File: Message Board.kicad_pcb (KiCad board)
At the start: 2 copper layers, 182.9 x 99.1 mm, 45 parts, among them J1 Conn_01x02, Q1 LGE2300, Q2 LGE2300, SW1 SW_SPST, U1 esp32-c3, U2 LM1117-5.0, U3 LM1117-3.3, U4 epaper75

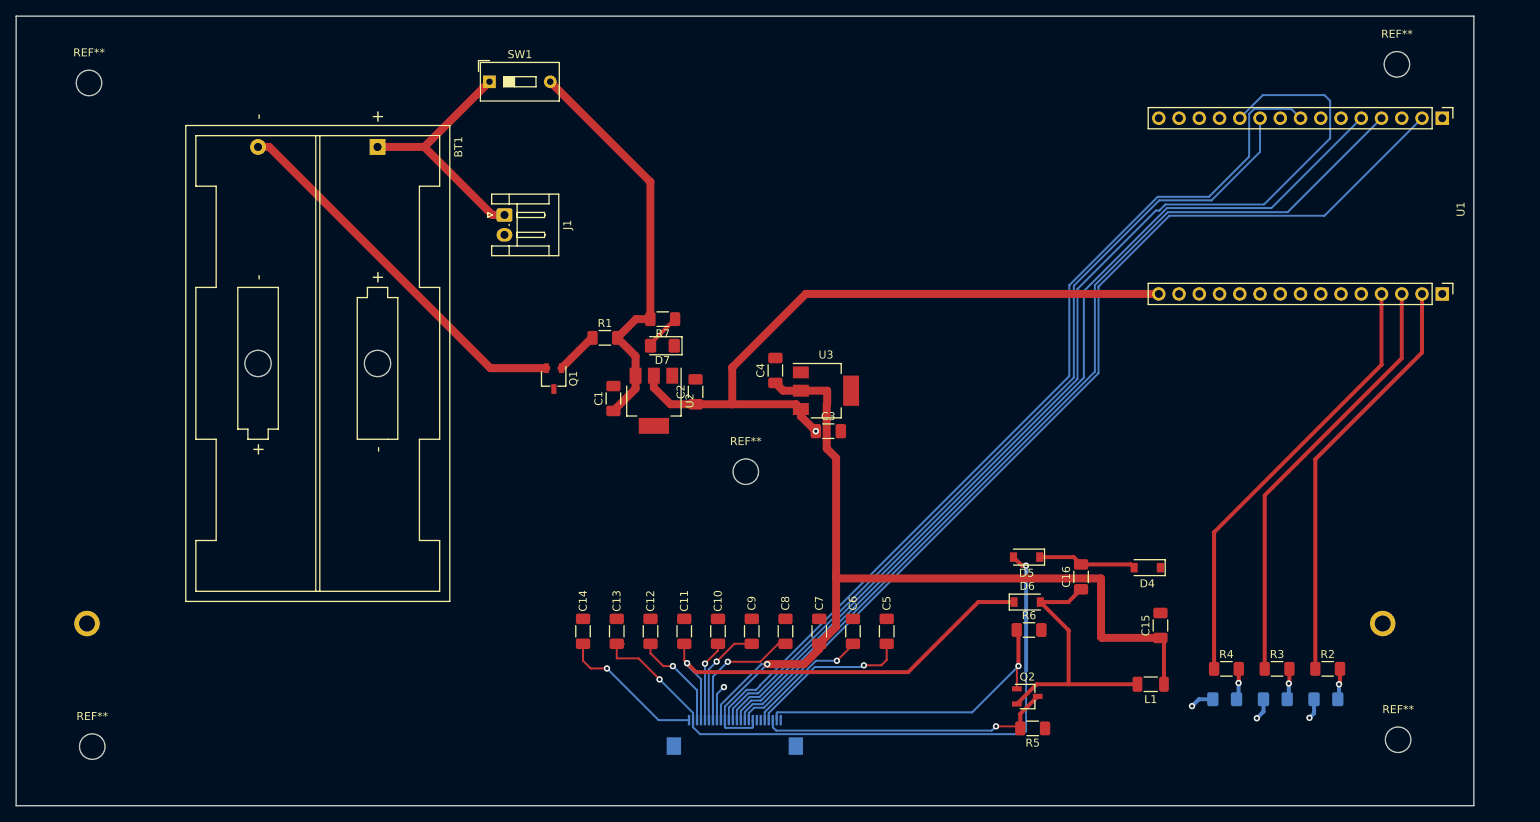
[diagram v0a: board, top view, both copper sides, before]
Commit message: Changed orientation of the FFC connector, battery from 2x18650 to 1x18650, devboard to ESP32-C3-DEVKITM-1 and updated the epaper footprint. Deleted second linear regualtor
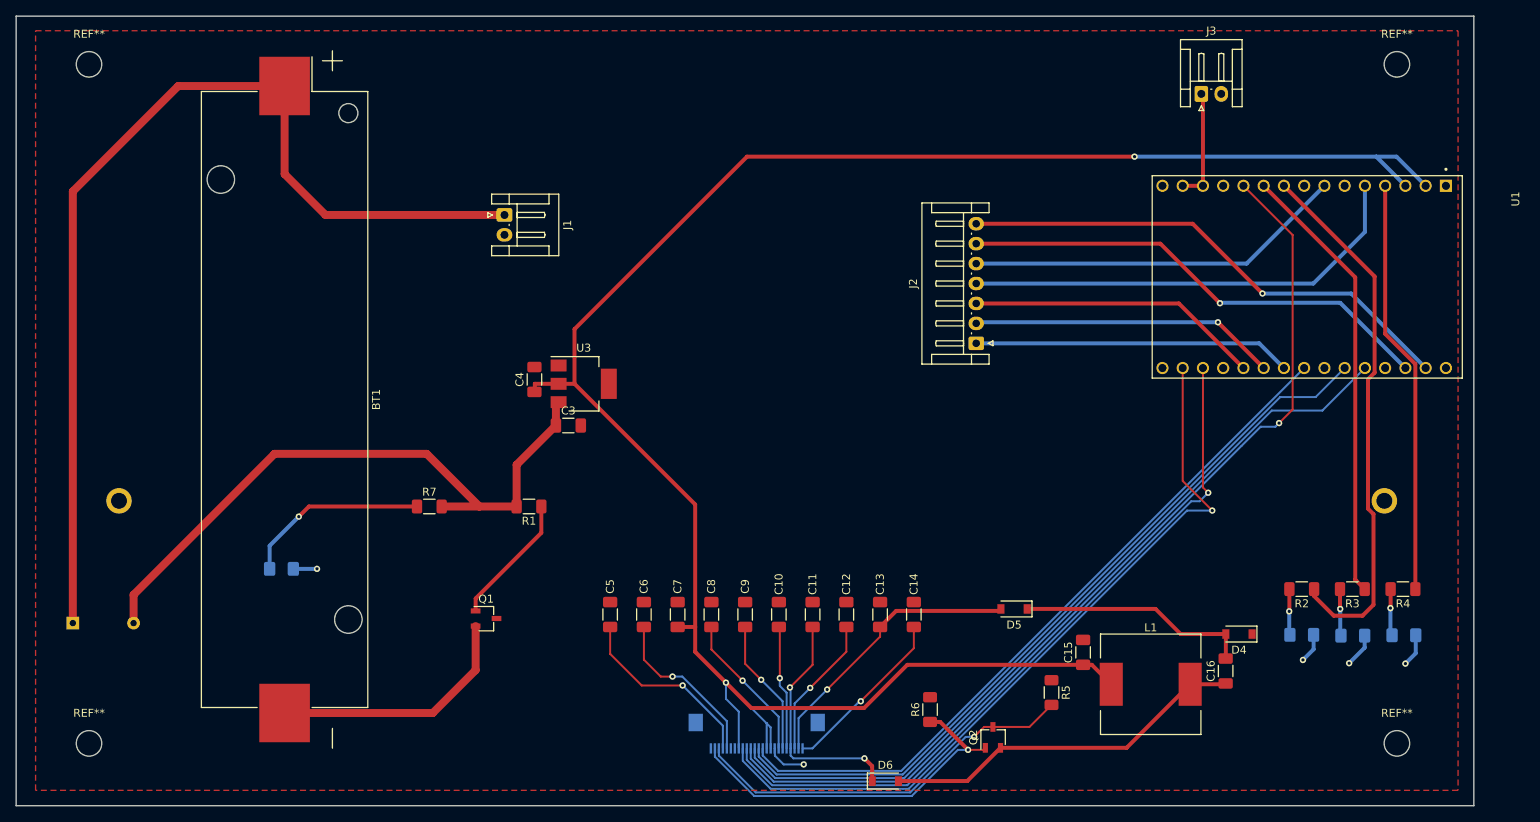
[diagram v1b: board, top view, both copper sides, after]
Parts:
- removed C1: 100nF, Capacitor_SMD:C_1206_3216Metric_Pad1.33x1.80mm_HandSolder
- removed C2: 10uF, Capacitor_SMD:C_1206_3216Metric_Pad1.33x1.80mm_HandSolder
- removed D3: LED, LED_SMD:LED_1206_3216Metric_Pad1.42x1.75mm_HandSolder
- removed the REF** at (162.7, 115.6)
- removed the REF** at (244.5, 149.2)
- removed the REF** at (80.7, 150.1)
- removed the REF** at (80.3, 66.8)
- removed U2: LM1117-5.0, Package_TO_SOT_SMD:SOT-223
- added D0: LED, LED_SMD:LED_1206_3216Metric_Pad1.42x1.75mm_HandSolder, B.Cu at (232.4, 136.0)
- added J2: Conn_01x07, Connector_JST:JST_EH_S7B-EH_1x07_P2.50mm_Horizontal, F.Cu at (191.6, 99.5)
- added J3: Conn_01x02, Connector_JST:JST_EH_S2B-EH_1x02_P2.50mm_Horizontal, F.Cu at (219.8, 68.2)
- added REF**: MountingHole_3.2mm_M3_DIN965, MountingHole:MountingHole_3.2mm_M3_DIN965, F.Cu at (244.3, 149.7)
- added REF**: MountingHole_3.2mm_M3_DIN965, MountingHole:MountingHole_3.2mm_M3_DIN965, F.Cu at (80.3, 149.7)
- added REF**: MountingHole_3.2mm_M3_DIN965, MountingHole:MountingHole_3.2mm_M3_DIN965, F.Cu at (80.3, 64.5)
- BT1: value 7.2 -> 3.6V; footprint Battery:BatteryHolder_Keystone_2462_2xAA -> Battery:BatteryHolder_Keystone_1042_1x18650
- D7, SW1: moved to B.Cu
- L1: footprint Inductor_SMD:L_1206_3216Metric_Pad1.22x1.90mm_HandSolder -> Inductor_SMD:L_12x12mm_H6mm
- U1: value esp32-c3 -> ESP32-C3-DEVKITM-1; footprint jw_lib:esp32-c3-s32-footprint -> jw_lib:XCVR_ESP32-C3-DEVKITM-1
- moved SW1 85.7 mm to (78.2, 134.6)
- moved D7 55.4 mm to (104.4, 127.8)
- moved C14 41.6 mm to (183.7, 133.5)
- moved R7 37.5 mm to (123.0, 119.9), turned to 0 degrees
- moved C5 34.8 mm to (145.6, 133.5)
- moved BT1 33.8 mm to (104.8, 106.5)
- moved C13 33.1 mm to (179.5, 133.5)
- moved C3 32.6 mm to (140.4, 109.8)
- moved Q1 31.3 mm to (130.1, 134.0), turned to 0 degrees
- moved U3 30.4 mm to (142.3, 104.5)
- moved C4 30.2 mm to (136.1, 104.0)
- moved D6 28.7 mm to (180.2, 154.4)
- moved C6 26.3 mm to (149.9, 133.5)
- moved U1 26.1 mm to (233.1, 91.1)
- moved C12 24.7 mm to (175.3, 133.5)
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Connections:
- C3 pad 1: /5V_OUT -> /BT_OUT
- R2 pad 1: /IO1 -> /IO0
- R2 pad 2: Net-(D1-Pad2) -> Net-(D0-Pad2)
- R3 pad 1: /IO2 -> /IO1
- R3 pad 2: Net-(D2-Pad2) -> Net-(D1-Pad2)
- R4 pad 1: /IO3 -> /IO2
- R4 pad 2: Net-(D3-Pad2) -> Net-(D2-Pad2)
- U1 pad 1: (no net) -> GND
- U1 pad 10: (no net) -> /IO1
- U1 pad 11: (no net) -> /EPD_DC
- U1 pad 12: (no net) -> GND
- U1 pad 13: (no net) -> Net-(J3-Pad1)
- U1 pad 14: GND -> Net-(J3-Pad1)
- U1 pad 15: /5V_OUT -> GND
- U1 pad 16: (no net) -> GND
- U1 pad 17: GND -> /EPD_BUSY
- U1 pad 18: (no net) -> /EPD_RST
- U1 pad 19: (no net) -> GND
- U1 pad 2: /IO1 -> /3.3V_OUT
- U1 pad 20: /EPD_CS -> Net-(J2-Pad3)
- U1 pad 21: /EPD_CLK -> Net-(J2-Pad2)
- U1 pad 22: (no net) -> Net-(J2-Pad1)
- U1 pad 25: (no net) -> /EPD_CLK
- U1 pad 26: /EPD_DC -> /EPD_CS
- U1 pad 27: /EPD_RST -> GND
- U1 pad 28: (no net) -> /RX
- U1 pad 29: /EPD_BUSY -> /LX
- U1 pad 3: /IO2 -> /3.3V_OUT
- U1 pad 30: (no net) -> GND
- U1 pad 4: /IO3 -> /IO2
- U1 pad 5: (no net) -> Net-(J2-Pad4)
- U1 pad 6: (no net) -> GND
- U1 pad 7: (no net) -> Net-(J2-Pad5)
- U1 pad 8: (no net) -> GND
- U1 pad 9: (no net) -> /IO0
- U3 pad 3: /5V_OUT -> /BT_OUT
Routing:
- net /3.3V_OUT: track 126.6 -> 258.4 mm, vias 1 -> 2
- net Net-(BT1-Pad1): track 31.0 -> 127.0 mm
- net /5V_OUT: track 86.6 -> 0.00 mm, vias 1 -> 0
- net /IO0: track 0.00 -> 67.8 mm
- net /LX: track 0.00 -> 63.9 mm, vias 0 -> 1
- net /RX: track 0.00 -> 60.4 mm, vias 0 -> 1
- net Net-(J2-Pad4): track 0.00 -> 57.2 mm
- net /IO3: track 55.7 -> 0.00 mm
- net Net-(J2-Pad5): track 0.00 -> 47.7 mm
- net /PREVGL: track 82.0 -> 35.6 mm, vias 2 -> 1
- net Net-(J2-Pad1): track 0.00 -> 39.9 mm
- net Net-(J2-Pad2): track 0.00 -> 38.5 mm, vias 0 -> 1
- net Net-(J2-Pad3): track 0.00 -> 36.9 mm
- net /BT_OUT: track 51.4 -> 81.5 mm
- net /EPD_CS: track 129.6 -> 100.1 mm
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- added copper zone on F.Cu, net GND

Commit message: Updated SPI connections, added hardware possibility to chose if 3 or 4 SPI version (BS Pin)
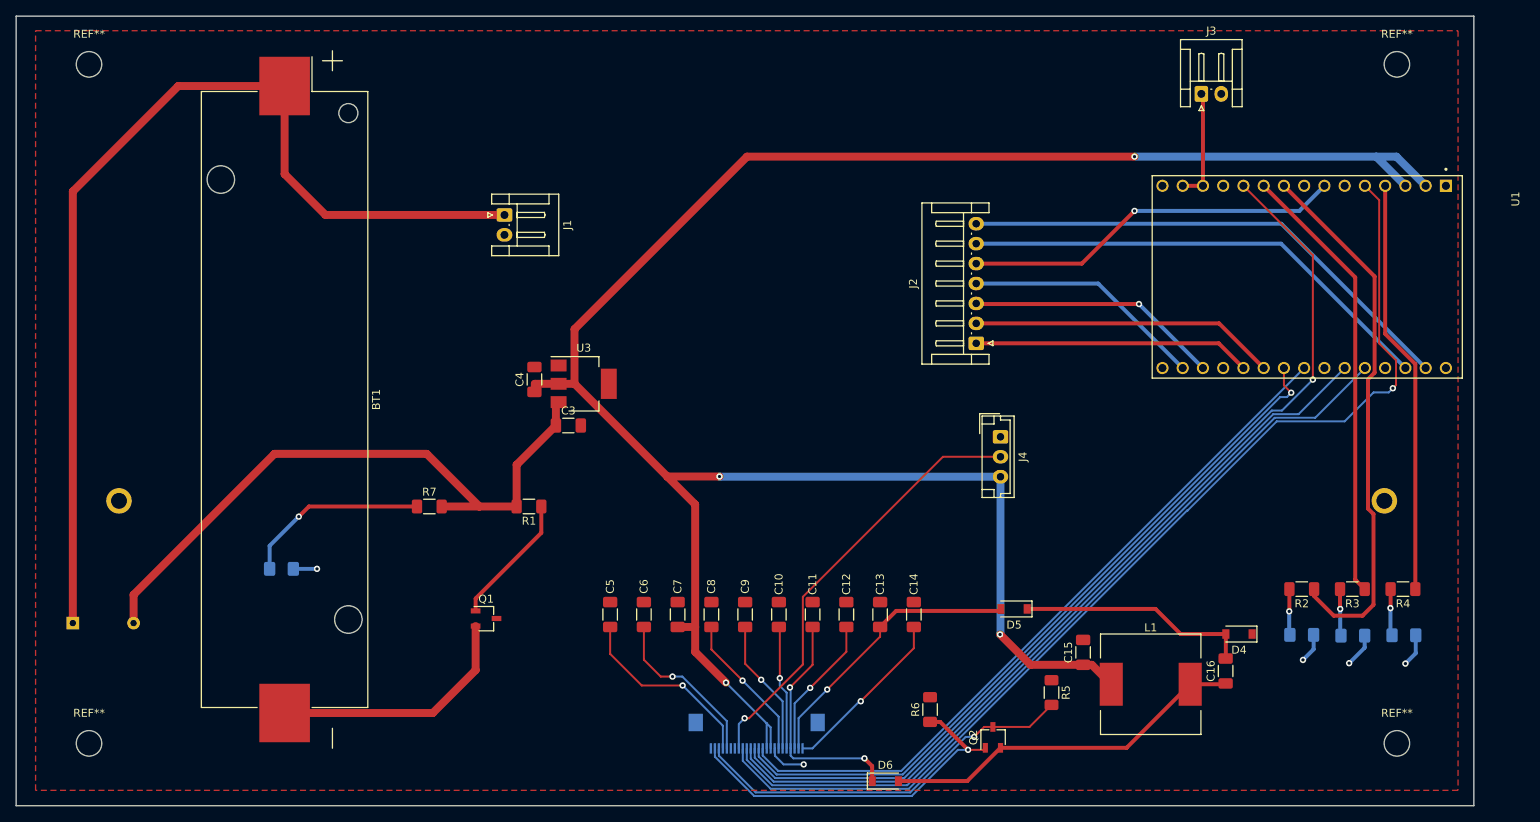
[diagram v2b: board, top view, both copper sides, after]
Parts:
- added J4: Conn_01x03, Connector_JST:JST_EH_B3B-EH-A_1x03_P2.50mm_Vertical, F.Cu at (194.6, 111.2)
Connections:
- net Net-(J2-Pad2) renamed /IO5
- net Net-(J2-Pad5) renamed /RST
- J2 pad 1: Net-(J2-Pad1) -> /IO4
- J2 pad 3: Net-(J2-Pad3) -> /IO18
- J2 pad 4: Net-(J2-Pad4) -> /IO19
- U1 pad 11: /EPD_DC -> /EPD_CS
- U1 pad 17: /EPD_BUSY -> /IO19
- U1 pad 18: /EPD_RST -> /IO18
- U1 pad 20: Net-(J2-Pad3) -> /IO4
- U1 pad 22: Net-(J2-Pad1) -> /EPD_CLK
- U1 pad 25: /EPD_CLK -> /EPD_DC
- U1 pad 26: /EPD_CS -> /EPD_RST
- U1 pad 5: Net-(J2-Pad4) -> /EPD_BUSY
- U4 pad 8: /3.3V_OUT -> /BS
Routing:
- net Net-(J2-Pad4): track 57.2 -> 0.00 mm
- net /BS: track 0.00 -> 54.7 mm, vias 0 -> 1
- net Net-(J2-Pad1): track 39.9 -> 0.00 mm
- net Net-(J2-Pad3): track 36.9 -> 0.00 mm
- net /EPD_BUSY: track 95.8 -> 132.6 mm
- net /IO4: track 0.00 -> 34.8 mm
- net /IO18: track 0.00 -> 31.8 mm, vias 0 -> 1
- net /IO19: track 0.00 -> 30.3 mm
- net /EPD_DC: track 120.4 -> 98.5 mm, vias 1 -> 0
- net /EPD_CS: track 100.1 -> 120.9 mm, vias 0 -> 1
- net /3.3V_OUT: track 258.4 -> 274.8 mm, vias 2 -> 4
- net /EPD_RST: track 91.8 -> 102.0 mm, vias 1 -> 0
- net /EPD_CLK: track 96.6 -> 92.1 mm, vias 0 -> 1
- net /IO5: track 38.5 -> 38.4 mm, vias 1 -> 0
- net /RX: track 60.4 -> 60.3 mm, vias 1 -> 0
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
